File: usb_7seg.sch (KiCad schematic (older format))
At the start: 11 parts, among them IC1 MAX7219CNG, IC2 MAX7219CWG, U1 SeeeduinoXIAO, U2 7segment_led, U3 7segment_led, U4 7segment_led, U5 7segment_led

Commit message: 0.36inchの7セグLEDを削除した
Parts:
- removed U3, U5: 7segment_led, kicad_7segment_led:kicad_7segment_led_0.56, symbol kicad_7segment_led:7segment_led
- U2, U4: footprint kicad_7segment_led:kicad_7segment_led_0.36 -> kicad_7segment_led:kicad_7segment_led_0.56
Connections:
- wire segments 257 -> 182
- no-connect marks 15 -> 17
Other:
- moved on the sheet: C1, C2

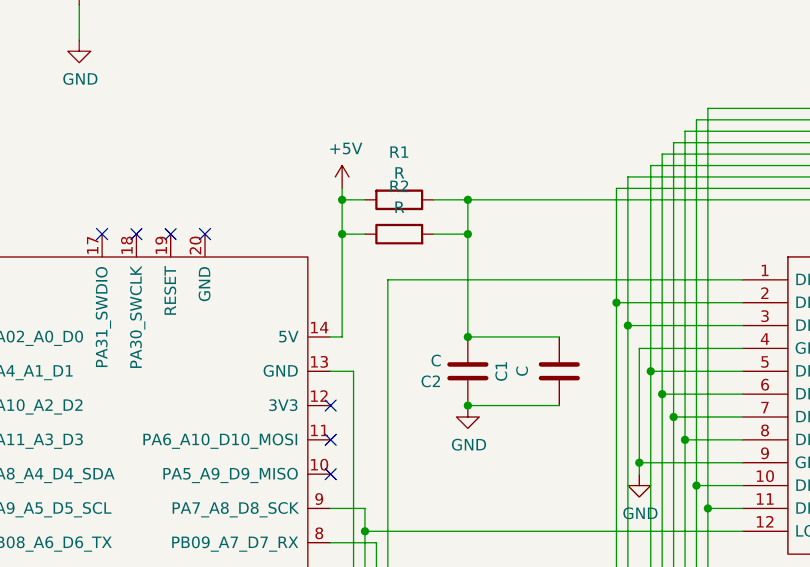
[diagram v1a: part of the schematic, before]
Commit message: C1,2が電源に繋がってなかった
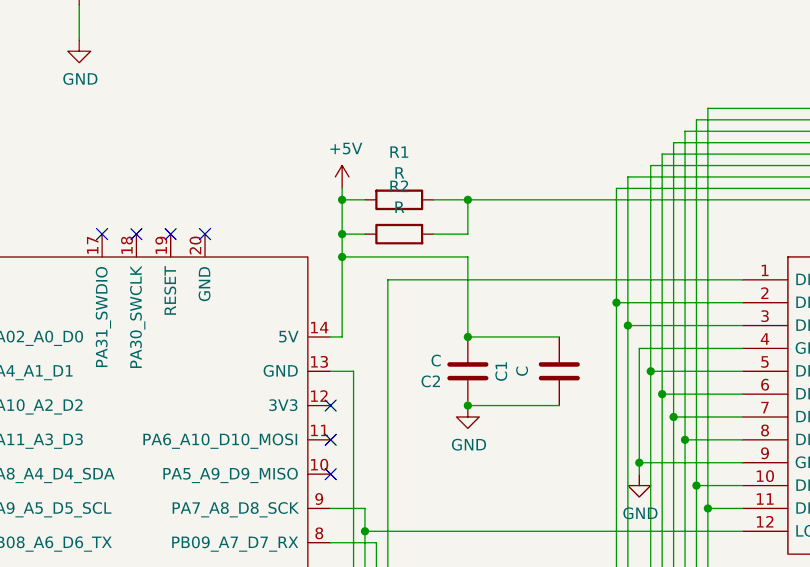
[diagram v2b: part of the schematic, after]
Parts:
- renumbered U4 to U3
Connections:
- wire segments 182 -> 184
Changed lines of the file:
@@
 $EndComp
 $Comp
-L kicad_7segment_led:7segment_led U4
+L kicad_7segment_led:7segment_led U3
 U 1 1 5EFD705B
 P 9750 2100
-F 0 "U4" H 9950 2275 50  0000 C CNN
+F 0 "U3" H 9950 2275 50  0000 C CNN
 F 1 "7segment_led" H 9950 2184 50  0000 C CNN
 F 2 "kicad_7segment_led:kicad_7segment_led_0.56" H 10150 2200 50  0001 C CNN
@@
 Wire Wire Line
 	2850 1800 2850 1950
-Wire Wire Line
-	3250 1800 3400 1800
 Wire Wire Line
 	6200 1800 6200 2750
@@
 Connection ~ 2850 1950
 Wire Wire Line
-	2850 1950 2850 2400
+	2850 1950 2850 2050
 Wire Wire Line
 	3250 1950 3400 1950
+NoConn ~ 2100 3700
+Wire Wire Line
+	3800 2400 3400 2400
+Connection ~ 3400 2700
+NoConn ~ 1900 3700
+Wire Wire Line
+	8950 2650 9650 2650
+Wire Wire Line
+	9200 2550 9650 2550
+Wire Wire Line
+	9150 2450 9650 2450
+Wire Wire Line
+	9050 2350 9650 2350
+Wire Wire Line
+	9000 2250 9650 2250
+Wire Wire Line
+	9100 2150 9650 2150
+Wire Wire Line
+	10250 2650 10750 2650
+Wire Wire Line
+	10250 2550 10850 2550
+Wire Wire Line
+	10250 2450 10800 2450
+Wire Wire Line
+	10250 2350 10700 2350
+Wire Wire Line
+	10250 2250 10650 2250
+Wire Wire Line
+	10250 2150 10900 2150
+Wire Wire Line
+	8100 2650 8650 2650
+Wire Wire Line
+	8100 2550 8750 2550
+Wire Wire Line
+	8100 2450 8700 2450
+Wire Wire Line
+	8100 2350 8600 2350
+Wire Wire Line
+	8100 2250 8550 2250
+Wire Wire Line
+	8100 2150 8800 2150
+Wire Wire Line
+	6700 2550 7500 2550
+Wire Wire Line
+	6750 2650 7500 2650
+Wire Wire Line
+	6650 2450 7500 2450
+Wire Wire Line
+	6550 2350 7500 2350
+Wire Wire Line
+	6500 2250 7500 2250
+Wire Wire Line
+	6600 2150 7500 2150
+Wire Wire Line
+	3250 1800 3400 1800
 Wire Wire Line
 	3400 1950 3400 1800
@@
 Wire Wire Line
 	3400 1800 6200 1800
-NoConn ~ 2100 3700
-Wire Wire Line
-	3800 2400 3400 2400
-Wire Wire Line
-	3400 1950 3400 2400
-Connection ~ 3400 1950
+Wire Wire Line
+	3400 2400 3400 2050
+Wire Wire Line
+	3400 2050 2850 2050
 Connection ~ 3400 2400
-Connection ~ 3400 2700
-NoConn ~ 1900 3700
-Wire Wire Line
-	8950 2650 9650 2650
-Wire Wire Line
-	9200 2550 9650 2550
-Wire Wire Line
-	9150 2450 9650 2450
-Wire Wire Line
-	9050 2350 9650 2350
-Wire Wire Line
-	9000 2250 9650 2250
-Wire Wire Line
-	9100 2150 9650 2150
-Wire Wire Line
-	10250 2650 10750 2650
-Wire Wire Line
-	10250 2550 10850 2550
-Wire Wire Line
-	10250 2450 10800 2450
-Wire Wire Line
-	10250 2350 10700 2350
-Wire Wire Line
-	10250 2250 10650 2250
-Wire Wire Line
-	10250 2150 10900 2150
-Wire Wire Line
-	8100 2650 8650 2650
-Wire Wire Line
-	8100 2550 8750 2550
-Wire Wire Line
-	8100 2450 8700 2450
-Wire Wire Line
-	8100 2350 8600 2350
-Wire Wire Line
-	8100 2250 8550 2250
-Wire Wire Line
-	8100 2150 8800 2150
-Wire Wire Line
-	6700 2550 7500 2550
-Wire Wire Line
-	6750 2650 7500 2650
-Wire Wire Line
-	6650 2450 7500 2450
-Wire Wire Line
-	6550 2350 7500 2350
-Wire Wire Line
-	6500 2250 7500 2250
-Wire Wire Line
-	6600 2150 7500 2150
+Connection ~ 2850 2050
+Wire Wire Line
+	2850 2050 2850 2400
 $EndSCHEMATC

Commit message: 7セグLEDを1つ削除した
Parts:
- removed U3: 7segment_led, kicad_7segment_led:kicad_7segment_led_0.56, symbol kicad_7segment_led:7segment_led
- U2: symbol kicad_7segment_led:7segment_led -> usb_7seg-rescue:7segment_led-kicad_7segment_led
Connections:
- wire segments 184 -> 139
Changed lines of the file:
@@
 $EndComp
 $Comp
-L kicad_7segment_led:7segment_led U2
+L usb_7seg-rescue:7segment_led-kicad_7segment_led U2
 U 1 1 5EFAF3F1
 P 7600 2100
@@
 	1    0    0    -1
 $EndComp
-$Comp
-L kicad_7segment_led:7segment_led U3
-U 1 1 5EFD705B
-P 9750 2100
-F 0 "U3" H 9950 2275 50  0000 C CNN
-F 1 "7segment_led" H 9950 2184 50  0000 C CNN
-F 2 "kicad_7segment_led:kicad_7segment_led_0.56" H 10150 2200 50  0001 C CNN
-F 3 "" H 10150 2200 50  0001 C CNN
-	1    9750 2100
-	1    0    0    -1
-$EndComp
-Wire Wire Line
-	10900 1700 10900 2150
 Wire Wire Line
 	6750 1550 6750 2650
 Wire Wire Line
-	8950 1500 8950 2650
-Wire Wire Line
-	10800 1450 10800 2450
-Wire Wire Line
 	8650 2950 8650 2650
 Wire Wire Line
@@
 	8550 3150 8550 2250
 Wire Wire Line
-	10850 1650 10850 2550
-Wire Wire Line
 	8700 1400 8700 2450
 Wire Wire Line
@@
 Wire Wire Line
 	8800 1750 8800 2150
-Wire Wire Line
-	10700 3050 10700 2350
-Wire Wire Line
-	10650 3150 10650 2250
 Wire Wire Line
 	6700 2850 6700 2550
@@
 	4050 1750 4050 2250
 Wire Wire Line
-	4100 1700 4100 2350
-Wire Wire Line
-	4200 1650 4200 2550
-Wire Wire Line
 	4250 1600 4250 2650
 Wire Wire Line
@@
 	4300 1550 6750 1550
 Wire Wire Line
-	4350 1500 4350 2850
-Wire Wire Line
-	4350 1500 8950 1500
-Wire Wire Line
-	4400 1450 4400 3050
-Wire Wire Line
 	4450 1400 4450 3150
-Wire Wire Line
-	6500 2250 6500 3200
-Wire Wire Line
-	6500 3200 9000 3200
-Wire Wire Line
-	9000 3200 9000 2250
 Connection ~ 6500 2250
-Wire Wire Line
-	6550 2350 6550 3250
-Wire Wire Line
-	6550 3250 9050 3250
-Wire Wire Line
-	9050 3250 9050 2350
 Connection ~ 6550 2350
-Wire Wire Line
-	6600 3300 9100 3300
-Wire Wire Line
-	9100 3300 9100 2150
 Connection ~ 6600 2450
 Wire Wire Line
-	6600 2450 6600 3300
-Wire Wire Line
 	6100 2550 6650 2550
-Wire Wire Line
-	6650 2550 6650 3350
-Wire Wire Line
-	6650 3350 9150 3350
-Wire Wire Line
-	9150 3350 9150 2450
 Connection ~ 6650 2550
-Wire Wire Line
-	6700 2850 6700 3400
-Wire Wire Line
-	6700 3400 9200 3400
-Wire Wire Line
-	9200 3400 9200 2550
 Connection ~ 6700 2850
 Wire Wire Line
-	4100 1700 10900 1700
-Wire Wire Line
-	4200 1650 10850 1650
-Wire Wire Line
-	4400 1450 10800 1450
-Wire Wire Line
-	10750 2650 10750 2950
-Wire Wire Line
 	4050 1750 8800 1750
 Wire Wire Line
@@
 Wire Wire Line
 	4450 1400 8700 1400
-Connection ~ 8550 3150
-Wire Wire Line
-	8550 3150 10650 3150
-Connection ~ 8600 3050
-Wire Wire Line
-	8600 3050 10700 3050
-Connection ~ 8650 2950
-Wire Wire Line
-	8650 2950 10750 2950
 Wire Wire Line
 	6100 2950 6350 2950
@@
 	3050 4550 1000 4550
 Wire Wire Line
-	6500 3200 6500 4150
-Wire Wire Line
 	6500 4150 5950 4150
-Connection ~ 6500 3200
 Wire Wire Line
 	5950 4250 6550 4250
 Wire Wire Line
-	6550 4250 6550 3250
-Connection ~ 6550 3250
-Wire Wire Line
-	6600 3300 6600 4350
-Wire Wire Line
 	6600 4350 5950 4350
-Connection ~ 6600 3300
-Wire Wire Line
-	6650 3350 6650 4450
 Wire Wire Line
 	6650 4450 5950 4450
-Connection ~ 6650 3350
-Wire Wire Line
-	6700 3400 6700 4750
 Wire Wire Line
 	6700 4750 5950 4750
-Connection ~ 6700 3400
 Wire Wire Line
 	5950 5050 6450 5050
@@
 Wire Wire Line
 	4400 4950 4750 4950
-Connection ~ 4400 3050
 Wire Wire Line
 	4750 4750 4350 4750
 Wire Wire Line
 	4350 4750 4350 2850
-Connection ~ 4350 2850
 Wire Wire Line
 	4300 2750 4300 4650
@@
 Wire Wire Line
 	4200 4450 4750 4450
-Connection ~ 4200 2550
 Wire Wire Line
 	4100 2350 4100 4250
 Wire Wire Line
 	4100 4250 4750 4250
-Connection ~ 4100 2350
 Wire Wire Line
 	4050 2250 4050 4150
@@
 NoConn ~ 1900 3700
 Wire Wire Line
-	8950 2650 9650 2650
-Wire Wire Line
-	9200 2550 9650 2550
-Wire Wire Line
-	9150 2450 9650 2450
-Wire Wire Line
-	9050 2350 9650 2350
-Wire Wire Line
-	9000 2250 9650 2250
-Wire Wire Line
-	9100 2150 9650 2150
-Wire Wire Line
-	10250 2650 10750 2650
-Wire Wire Line
-	10250 2550 10850 2550
-Wire Wire Line
-	10250 2450 10800 2450
-Wire Wire Line
-	10250 2350 10700 2350
-Wire Wire Line
-	10250 2250 10650 2250
-Wire Wire Line
-	10250 2150 10900 2150
-Wire Wire Line
 	8100 2650 8650 2650
 Wire Wire Line
@@
 Wire Wire Line
 	2850 2050 2850 2400
+Wire Wire Line
+	6500 2250 6500 4150
+Wire Wire Line
+	6550 2350 6550 4250
+Wire Wire Line
+	6600 2450 6600 4350
+Wire Wire Line
+	6650 2550 6650 4450
+Wire Wire Line
+	6700 2850 6700 4750
 $EndSCHEMATC

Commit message: フットプリントの関連付けを修正
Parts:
- U1: footprint Seeeduino XIAO:Seeeduino XIAO-MOUDLE14P-2.54-21X17.8MM -> kicad_mylib:SeeedXIAO
- U2: footprint kicad_7segment_led:kicad_7segment_led_0.56 -> kicad_mylib:7segment_led_0.56
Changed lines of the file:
@@
 F 0 "U1" H 1975 1911 50  0000 C CNN
 F 1 "SeeeduinoXIAO" H 1975 1820 50  0000 C CNN
-F 2 "Seeeduino XIAO:Seeeduino XIAO-MOUDLE14P-2.54-21X17.8MM" H 1650 3050 50  0001 C CNN
+F 2 "kicad_mylib:SeeedXIAO" H 1650 3050 50  0001 C CNN
 F 3 "" H 1650 3050 50  0001 C CNN
 	1    2000 2850
@@
 F 0 "U2" H 7800 2275 50  0000 C CNN
 F 1 "7segment_led" H 7800 2184 50  0000 C CNN
-F 2 "kicad_7segment_led:kicad_7segment_led_0.56" H 8000 2200 50  0001 C CNN
+F 2 "kicad_mylib:7segment_led_0.56" H 8000 2200 50  0001 C CNN
 F 3 "" H 8000 2200 50  0001 C CNN
 	1    7600 2100

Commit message: 配置配線、ERC ok
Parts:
- removed IC1: MAX7219CNG, MAX7219CNG:MAX7219CNG, symbol MAX7219CNG:MAX7219CNG
- removed IC2: MAX7219CWG, MAX7219CWG:MAX7219CWG, symbol MAX7219CWG:MAX7219CWG
- added U3: TM1637, kicad_mylib:TM1630, symbol kicad_mylib:TM1637
- C1, C2: value C -> 10uF
- R1: value R -> 10k
- R2: value R -> 10k; footprint Resistor_SMD:R_0805_2012Metric_Pad1.15x1.40mm_HandSolder -> Resistor_THT:R_Axial_DIN0207_L6.3mm_D2.5mm_P10.16mm_Horizontal
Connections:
- net +5V: now also R1.1, U3.VDD (16); no longer R1.2
- net GND: now also U3.GND (1)
- net at U2.9 (C2): now also U3.GRID2 (14)
- net at U1.9 (PA7_A8_D8_SCK): now also R1.2, U3.DIO (17)
- net at U1.8 (PB09_A7_D7_RX): now also R2.2, U3.CLK (18)
- net at U2.11 (A): now also U3.SEG1 (2)
- net at U2.10 (F): now also U3.SEG6 (7)
- net at U2.7 (B): now also U3.SEG2 (3)
- net at U2.5 (G): now also U3.SGE7 (8)
- net at U2.12 (C1): now also U3.GRID1 (15)
- net at U2.4 (C): now also U3.SEG3 (4)
- net at U2.1 (E): now also U3.SEG5 (6)
- net at U2.3 (DP): now also U3.SEG8 (9)
- net at U2.2 (D): now also U3.SEG4 (5)
- net at U2.8 (C3): now also U3.GRID3 (13)
- net at U2.6 (C4): now also U3.GRID4 (12)
- no-connect marks 17 -> 20
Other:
- moved on the sheet: C1, C2, U1, U2
